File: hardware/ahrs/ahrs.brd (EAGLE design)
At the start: 32 x 30 mm, 38 parts, among them J1 2-PIN, J2 3-PIN3, J3 SM08B-SRSS-TB, U1 LSM9DS1, U2 STM32G4_UFQFPN48_T1, U3 LDFM33PUR, U4 MCP2542FD, X1 NX2016SA24MHZ-EXS00A-CS11335

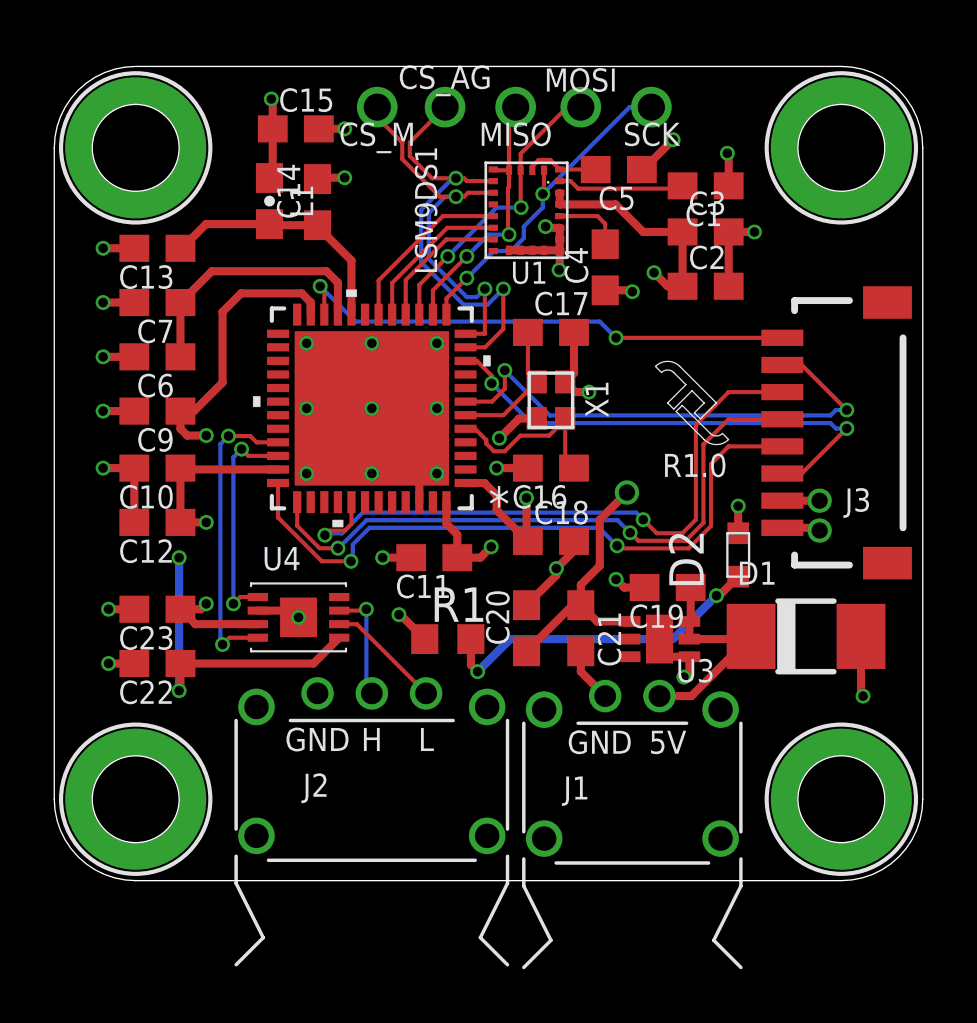
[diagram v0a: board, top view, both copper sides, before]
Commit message: Added LEDs and updates for PCBway
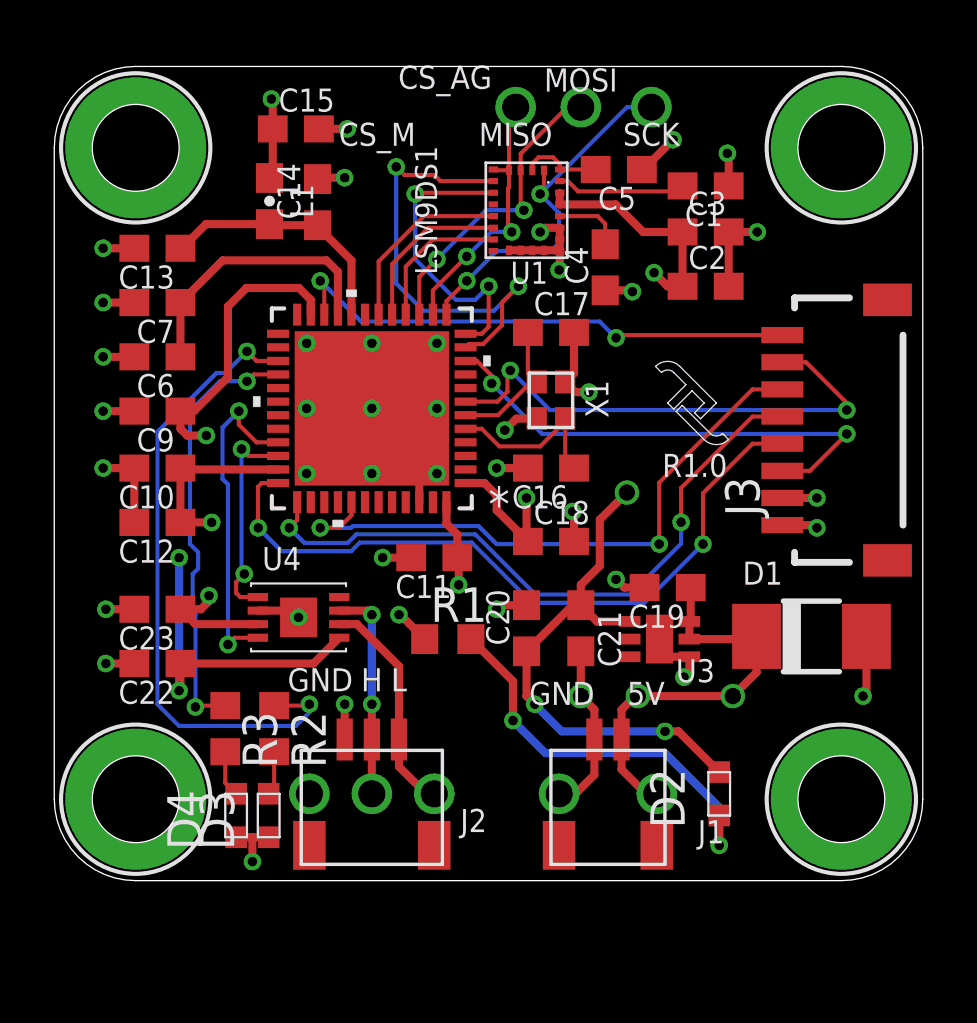
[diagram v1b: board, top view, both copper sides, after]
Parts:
- added D3, D4: LED_0603150060RS75000, timlib:D0603
- added R2, R3: 68, rcl:R0603
- J1: value 2-PIN -> LINEAR_2_JST_SH_RA; device timlib:M80-8420242 -> _T_conn:JST_SM02B-SRSS-TB
- J2: value 3-PIN3 -> LINEAR_3_JST_PH_RA; device timlib:M80-8430342 -> _T_conn:JST_SM03B-SRSS-TB
- J3: value SM08B-SRSS-TB -> LINEAR_8_JST_PH_RA; device timlib:SM08B-SRSS-TB -> _T_conn:JST_SM08B-SRSS-TB
- moved D2 8.83 mm to (24.5, 3.20)
- moved J1 2.56 mm to (20.4, 4.40)
- moved J2 2.50 mm to (11.7, 4.40)
- moved D1 0.20 mm to (27.9, 9.00)
- moved J3 0.10 mm to (29.8, 16.6)
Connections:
- new net N$10: R3.1, U2.28
- new net N$7: R2.1, U2.27
- new net N$8: D3.2, R2.2
- new net N$9: D4.2, R3.2
- net GND: now also D3.1, D4.1
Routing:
- net N$7: track 0.00 -> 23.6 mm, vias 0 -> 2
- net N$10: track 0.00 -> 16.1 mm, vias 0 -> 2
- net 3.3V: track 63.1 -> 72.0 mm, vias 12 -> 13
- net GND: track 47.2 -> 54.4 mm, vias 34 -> 40
- net 5V: track 12.6 -> 19.6 mm, vias 1 -> 4
- net CAN_L: track 4.26 -> 8.26 mm, vias 0 -> 1
- net CAN_H: track 4.20 -> 7.86 mm, vias 1 -> 3
- net CS_M: track 14.4 -> 11.3 mm, vias 3 -> 2
- net N$1: track 12.4 -> 15.1 mm
- net SWDIO: track 24.6 -> 26.6 mm
- net N$9: track 0.00 -> 1.72 mm
- net N$8: track 0.00 -> 1.63 mm
- net SCK: track 12.5 -> 14.0 mm
- net CAN_RX: track 11.2 -> 12.3 mm
- net SWCLK: track 23.4 -> 24.4 mm
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
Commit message: Oops, removed CS_(AG|M) pads
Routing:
- net CS_M: track 11.3 -> 15.5 mm, vias 2 -> 3
- net CS_AG: track 16.7 -> 19.7 mm, vias 2 -> 3
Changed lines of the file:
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@@
 </layers>
 <board>
+<fusionsync huburn="a.YnVzaW5lc3M6Z21haWwyMjE5MTc" projecturn="a.YnVzaW5lc3M6Z21haWwyMjE5MTcjMjAxOTA2MjkyMDE0MTU5NzY" f3durn="urn:adsk.wipprod:dm.lineage:MzfWSGJQS0CBInJEB5SxYw" pcbguid="" lastpulledtime="" lastsyncedchangeguid="" latestrevisionid="cad069d0-54c5-44df-b114-c58309e67b1b" lastsyncedrevisionid="cad069d0-54c5-44df-b114-c58309e67b1b" lastboardhashguid="3784b1de-b935-57e8-db1c-6b4475f25a4e" lastpushedtime="2020-04-26T23:37:28Z" linktopcb3d="%12"/>
 <plain>
 <circle x="3" y="3" radius="2.75" width="0.1524" layer="21"/>
@@
 <circle x="29" y="27" radius="2.75" width="0.1524" layer="21"/>
 <circle x="3" y="27" radius="2.75" width="0.1524" layer="21"/>
-<text x="11.9" y="27.5" size="0.85" layer="25" align="center">CS_M</text>
-<text x="14.4" y="29.6" size="0.85" layer="25" align="center">CS_AG</text>
+<text x="12" y="25.9" size="0.85" layer="25" rot="R90" align="center">CS_M</text>
+<text x="14.4" y="25.7" size="0.85" layer="25" rot="R90" align="center">CS_AG</text>
 <text x="17" y="27.5" size="0.85" layer="25" align="center">MISO</text>
 <text x="19.4" y="29.5" size="0.85" layer="25" align="center">MOSI</text>
@@
 <element name="U1" library="timlib" library_urn="urn:adsk.eagle:library:16152524" package="LGA24_3.5X3X1" package3d_urn="urn:adsk.eagle:package:18130566/2" value="LSM9DS1" x="17.4" y="24.7" smashed="yes" rot="R270">
 <attribute name="NAME" x="17.5" y="22.4" size="0.8128" layer="21" align="center"/>
-<attribute name="VALUE" x="13.7" y="24.7" size="0.8128" layer="21" rot="R270" align="center"/>
 </element>
 <element name="U2" library="timlib" library_urn="urn:adsk.eagle:library:16152524" package="UFQFPN-48_7X7X0P55MM" package3d_urn="urn:adsk.eagle:package:19324073/5" value="STM32G4_UFQFPN48_T1" x="11.7" y="17.4" smashed="yes" rot="R180">
@@
 <via x="17.4" y="14.1" extent="1-16" drill="0.35"/>
 <wire x1="19.4" y1="10.15" x2="19.4" y2="10.9" width="0.3" layer="1"/>
-<wire x1="19.4" y1="10.9" x2="20.1" y2="11.6" width="0.3" layer="1"/>
+<wire x1="19.4" y1="10.9" x2="20.4" y2="11.9" width="0.3" layer="1"/>
 <wire x1="21.2" y1="9.55" x2="20" y2="9.55" width="0.3" layer="1"/>
 <wire x1="20" y1="9.55" x2="19.4" y2="10.15" width="0.3" layer="1"/>
@@
 <wire x1="21.7" y1="26.2" x2="22.8" y2="27.3" width="0.3" layer="1"/>
 <via x="22.8" y="27.3" extent="1-16" drill="0.35"/>
-<wire x1="20.1" y1="13.3" x2="21.1" y2="14.3" width="0.3" layer="1"/>
+<wire x1="20.4" y1="13.6" x2="21.1" y2="14.3" width="0.3" layer="1"/>
 <via x="21.1" y="14.3" extent="1-16" drill="0.6"/>
-<wire x1="20.1" y1="11.6" x2="20.1" y2="13.3" width="0.3" layer="1"/>
+<wire x1="20.4" y1="11.9" x2="20.4" y2="13.6" width="0.3" layer="1"/>
 <contactref element="D2" pad="2"/>
 <wire x1="4.65" y1="8" x2="4.65" y2="7.05" width="0.3" layer="1"/>
@@
 <wire x1="14" y1="26" x2="14.225" y2="25.775" width="0.1524" layer="1"/>
 <wire x1="14.225" y1="25.775" x2="16.175" y2="25.775" width="0.1524" layer="1"/>
+<via x="14.5" y="28.5" extent="1-16" drill="1" alwaysstop="yes"/>
+<wire x1="12.6" y1="26.3" x2="14.5" y2="28.2" width="0.1524" layer="16"/>
+<wire x1="14.5" y1="28.2" x2="14.5" y2="28.5" width="0.1524" layer="16"/>
 </signal>
 <signal name="CS_M">
@@
 <wire x1="16" y1="20.4" x2="15.75" y2="20.15" width="0.1524" layer="1"/>
 <wire x1="15.75" y1="20.15" x2="15.1544" y2="20.15" width="0.1524" layer="1"/>
+<via x="12" y="28.5" extent="1-16" drill="1" alwaysstop="yes"/>
+<wire x1="13.3" y1="25.3" x2="12.4" y2="25.3" width="0.1524" layer="1"/>
+<wire x1="12" y1="25.7" x2="12" y2="28.5" width="0.1524" layer="1"/>
+<wire x1="12.4" y1="25.3" x2="12" y2="25.7" width="0.1524" layer="1"/>
 </signal>
 <signal name="SCK">
@@
 </note>
 <note version="8.3" severity="warning">
+Since Version 8.3, EAGLE supports Fusion synchronisation.
+This feature will not be available in this version and saving
+the document will break the link to the Fusion PCB feature.
+</note>
+<note version="8.3" severity="warning">

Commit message: POSSIBLY BAD MERGE
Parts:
- removed H1, H2, H3, H4: GND_HOLE_M3, timlib:HOLE_GND_M3
- removed J2: LINEAR_3_JST_PH_RA, _T_conn:JST_SM03B-SRSS-TB
- added C8: 0.1uF 10V, _T_rcl:C0603
- added J4: LINEAR_35040500391, _T_conn:MOLEX_5040500391
- added L2: 600R@100MHz, _T_rcl:L0603
- added R4: (no value), _T_rcl:R0603
- C1, C10, C13, C15, C3, C5, C6, C9: value 100nF 10v -> 0.1uF 10V; device rcl:C0603 -> _T_rcl:C0603
- C11, C12, C14, C18, C19, C2, C22, C23, C4, C7: device rcl:C0603 -> _T_rcl:C0603
- C16, C17: value 6.2pF 10v -> 10pF 10v; device rcl:C0603 -> _T_rcl:C0603
- C20, C21: value 22uF 10v -> 2.2uF 10V; device rcl:C0603 -> _T_rcl:C0603
- D1: value SMAJ5A -> (none); device timlib:DO-214AC -> _T_rcl:SOD123
- D2, D3, D4: value LED_0603150060RS75000 -> 150060BS75000; device timlib:D0603 -> _T_rcl:D0603
- J1: value LINEAR_2_JST_SH_RA -> LINEAR_2_5040500291; device _T_conn:JST_SM02B-SRSS-TB -> _T_conn:MOLEX_5040500291
- J3: value LINEAR_8_JST_PH_RA -> LINEAR_85040500891; device _T_conn:JST_SM08B-SRSS-TB -> _T_conn:MOLEX_5040500891
- L1: device timlib:L0603 -> _T_rcl:L0603
- R1, R2, R3: value 68 -> 22; device rcl:R0603 -> _T_rcl:R0603
- U1: device timlib:LGA24_3.5X3X1 -> _T_ic:LGA24_3.5X3X1
- U2: device timlib:UFQFPN-48_7X7X0P55MM -> _T_ic:UFQFPN-48_7X7X0P55MM
- U3: device timlib:DFN6_2X2 -> _T_ic:DFN6_2X2
- U4: device timlib:TDFN_2X3 -> _T_ic:TDFN_2X3
- X1: value NX2016SA24MHZ-EXS00A-CS11335 -> CRYSTAL_NX2016SA-24MHZ-EXS00A-CS11335; device timlib:NX201SA -> _T_ic:NX201SA
- moved D4 22.6 mm to (28.2, 9.50), turned to 0 degrees
- moved D3 22.1 mm to (28.2, 11.2), turned to 0 degrees
- moved R3 18.7 mm to (24.6, 9.50), turned to 0 degrees
- moved R2 17.4 mm to (24.6, 11.2), turned to 0 degrees
- moved C22 16.7 mm to (20.0, 12.2), turned to 270 degrees
- moved J3 16.4 mm to (15.0, 23.6), turned to 0 degrees
- moved U3 15.7 mm to (6.70, 10.3), turned to 270 degrees
- moved C19 15.6 mm to (7.20, 8.20)
- moved C4 11.3 mm to (27.3, 13.7), turned to 0 degrees
- moved R1 10.2 mm to (24.6, 7.80), turned to 180 degrees
- moved C21 9.61 mm to (9.80, 9.80), turned to 180 degrees
- moved C12 9.45 mm to (7.50, 21.9), turned to 270 degrees
- moved U4 9.42 mm to (18.4, 9.10), turned to 90 degrees
- moved C9 8.26 mm to (2.20, 9.20), turned to 0 degrees
- moved C15 8.02 mm to (2.20, 23.3), turned to 180 degrees
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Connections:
- removed net 3.3V: C10.1, C11.1, C12.1, C15.1, C18.1, C2.1, C20.1, C21.1, C22.1, C3.1, C5.1, C9.1, D2.2, J3.1, L1.1, U1.P$22, U1.P$23, U2.1, U2.23, U2.35, U2.48, U3.PIN1, U4.5
- removed net 5V: C19.1, C23.1, D1.C, J1.1, U3.PIN5, U3.PIN6, U4.3
- removed net CAN_H: J2.2, U4.7
- removed net CAN_L: J2.1, U4.6
- removed net INT1_AG: U1.P$11, U2.17
- removed net INT2_AG: U1.P$12, U2.16
- removed net INT_M: U1.P$10, U2.18
- new net +3V3: C10.1, C11.1, C12.1, C15.1, C18.1, C2.1, C20.1, C21.1, C22.1, C3.1, C5.1, C8.1, C9.1, D2.2, J3.P1, L1.1, L2.2, U1.P$22, U1.P$23, U2.1, U2.23, U2.35, U2.48, U3.PIN1, U4.5
- new net +5V: C19.1, C23.1, D1.C, J1.P1, U3.PIN5, U3.PIN6, U4.3
- new net N$11: J4.P1, R4.2, U4.7
- new net N$12: J4.P2, R4.1, U4.6
- net GND: now also C8.2, J1.P2, J3.P2, J4.P3, R2.2, R3.2, U4.8; no longer D3.1, D4.1, H1.P$1, H2.P$1, H3.P$1, H4.P$1, J1.2, J2.3, J3.2
- net LPUART_RX: now also J3.P8; no longer J3.8
- net LPUART_TX: now also J3.P3; no longer J3.3
- net N$10: now also D4.1; no longer U2.28
- net N$7: now also D4.2, U2.28; no longer R2.1, U2.27
- net N$8: now also U2.26; no longer R2.2
- net N$9: now also D3.1, R2.1; no longer D4.2, R3.2
- net NRST: now also J3.P7; no longer J3.7
- net SWCLK: now also J3.P5; no longer J3.5
- net SWDIO: now also J3.P4; no longer J3.4
- net SWO: now also J3.P6; no longer J3.6
- net VDDA: now also L2.1
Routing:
- net 3.3V: track 72.0 -> 0.00 mm, vias 13 -> 0
- net +3V3: track 0.00 -> 50.7 mm, vias 0 -> 14
- net N$8: track 1.63 -> 43.2 mm, vias 0 -> 2
- net +5V: track 0.00 -> 33.9 mm
- net 5V: track 19.6 -> 0.00 mm, vias 4 -> 0
- net N$7: track 23.6 -> 42.3 mm
- net N$10: track 16.1 -> 2.05 mm, vias 2 -> 0
- net CAN_TX: track 7.78 -> 21.7 mm
- net N$1: track 15.1 -> 2.05 mm, vias 2 -> 0
- net SWDIO: track 26.6 -> 14.4 mm
- net CS_AG: track 19.7 -> 7.75 mm, vias 3 -> 2
- net CAN_RX: track 12.3 -> 23.2 mm
- net SWCLK: track 24.4 -> 15.6 mm
- net NRST: track 18.8 -> 10.1 mm
- net CS_M: track 15.5 -> 6.90 mm, vias 3 -> 2
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- added copper zone on layer 2, net +3V3
- removed copper zone on layer 2, net 3.3V
- removed copper zone on layer 2, net 5V
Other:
- board size 32 x 30 mm -> 30 x 30 mm
- board text removed: "5V"
- board text removed: "CS_AG"
- board text removed: "CS_M"
- board text removed: "GND"
- board text removed: "H"
- board text removed: "L"
- board text removed: "MISO"
- board text removed: "MOSI"
- board text removed: "R1.0"
- board text removed: "SCK"

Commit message: Initial Power v3
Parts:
- C2: value 10uF 10v -> 10uF 10V
- moved C2 0.10 mm to (27.3, 15.9)
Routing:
- net +3V3: track 50.7 -> 49.9 mm, vias 14 -> 13
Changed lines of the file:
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@@
 </layers>
 <board>
-<fusionsync huburn="a.YnVzaW5lc3M6Z21haWwyMjE5MTc" projecturn="a.YnVzaW5lc3M6Z21haWwyMjE5MTcjMjAxOTA2MjkyMDE0MTU5NzY" f3durn="urn:adsk.wipprod:dm.lineage:MzfWSGJQS0CBInJEB5SxYw" pcbguid="" lastpulledtime="" lastsyncedchangeguid="" latestrevisionid="2e79b3d6-53ce-43aa-848e-6e5a329550ac" lastsyncedrevisionid="2e79b3d6-53ce-43aa-848e-6e5a329550ac" lastboardhashguid="9ffdacb0-3b78-cc97-8a35-4617afdf7dd1" lastpushedtime="2020-06-01T07:50:32Z" linktopcb3d="%12"/>
+<fusionsync huburn="a.YnVzaW5lc3M6Z21haWwyMjE5MTc" projecturn="a.YnVzaW5lc3M6Z21haWwyMjE5MTcjMjAxOTA2MjkyMDE0MTU5NzY" f3durn="urn:adsk.wipprod:dm.lineage:MzfWSGJQS0CBInJEB5SxYw" pcbguid="" lastpulledtime="" lastsyncedchangeguid="" latestrevisionid="479aee42-1d56-4d93-9275-ec8a74ec2958" lastsyncedrevisionid="479aee42-1d56-4d93-9275-ec8a74ec2958" lastboardhashguid="e3f8bce3-a763-ae1a-6ea7-c9e59d677afc" lastpushedtime="2020-06-02T04:09:23Z" linktopcb3d="%12"/>
 <plain>
 <circle x="3" y="3" radius="2.75" width="0.1524" layer="21"/>
@@
 <attribute name="VALUE" x="2.835" y="25.205" size="1.27" layer="27" rot="R180"/>
 </element>
-<element name="C2" library="_T_rcl" library_urn="urn:adsk.eagle:library:19571919" package="C0603" package3d_urn="urn:adsk.eagle:package:19572011/3" override_package3d_urn="urn:adsk.eagle:package:19477979/2" override_package_urn="urn:adsk.eagle:footprint:23123/1" override_locally_modified="yes" value="10uF 10v" x="27.3" y="15.8" smashed="yes" rot="R180">
-<attribute name="NAME" x="29.1" y="15.8" size="0.8" layer="25" rot="R180" align="center"/>
-<attribute name="VALUE" x="27.935" y="17.705" size="1.27" layer="27" rot="R180"/>
-</element>
 <element name="C3" library="_T_rcl" library_urn="urn:adsk.eagle:library:19571919" package="C0603" package3d_urn="urn:adsk.eagle:package:19572011/3" value="0.1uF 10V" x="27.3" y="17.8" smashed="yes" rot="R180">
 <attribute name="NAME" x="29.1" y="17.8" size="0.8" layer="25" rot="R180" align="center"/>
@@
 <attribute name="NAME" x="19.97" y="2.07" size="0.8" layer="25" rot="R180" align="center"/>
 <attribute name="VALUE" x="19.97" y="3.67" size="0.9" layer="27" rot="R180" align="center"/>
+</element>
+<element name="C2" library="_T_rcl" library_urn="urn:adsk.eagle:library:19571919" package="C0603" package3d_urn="urn:adsk.eagle:package:19572011/3" value="10uF 10V" x="27.3" y="15.9" smashed="yes" rot="R180">
+<attribute name="NAME" x="29.17" y="15.93" size="0.8" layer="25" rot="R180" align="center"/>
+<attribute name="VALUE" x="28.57" y="18.44" size="1.27" layer="27" rot="R180"/>
 </element>
 </elements>
@@
 <contactref element="U1" pad="P$16"/>
 <contactref element="U1" pad="P$18"/>
-<contactref element="C2" pad="2"/>
 <contactref element="C3" pad="2"/>
 <contactref element="X1" pad="P$4"/>
@@
 <via x="3.7" y="23.3" extent="1-16" drill="0.29"/>
 <wire x1="1.45" y1="17.4" x2="1.45" y2="19.5" width="0.3" layer="1"/>
-<wire x1="1.45" y1="17.4" x2="0.5474" y2="17.4" width="0.3" layer="1"/>
-<via x="0.5474" y="17.4" extent="1-16" drill="0.29"/>
-<wire x1="28.05" y1="15.8" x2="28.05" y2="17.8" width="0.3" layer="1"/>
+<wire x1="1.45" y1="17.4" x2="0.7" y2="17.4" width="0.3" layer="1"/>
+<via x="0.7" y="17.4" extent="1-16" drill="0.29"/>
 <wire x1="28.05" y1="17.8" x2="28.05" y2="18.65" width="0.3" layer="1"/>
 <wire x1="28.05" y1="18.65" x2="28.2" y2="18.8" width="0.3" layer="1"/>
@@
 <wire x1="18.225" y1="18.475" x2="18.225" y2="19.375" width="0.3" layer="1"/>
 <wire x1="18.225" y1="19.375" x2="18.55" y2="19.7" width="0.3" layer="1"/>
+<contactref element="C2" pad="2"/>
+<wire x1="28.05" y1="15.9" x2="28.05" y2="17.8" width="0.3" layer="1"/>
 </signal>
 <signal name="N$2">
@@
 <contactref element="L1" pad="1"/>
 <contactref element="U1" pad="P$22"/>
-<contactref element="C2" pad="1"/>
 <contactref element="C3" pad="1"/>
 <contactref element="U1" pad="P$23"/>
@@
 <wire x1="28.1" y1="22.05" x2="28.1" y2="21.1" width="0.3" layer="1"/>
 <via x="28.1" y="21.1" extent="1-16" drill="0.29"/>
-<wire x1="26.55" y1="17.8" x2="26.55" y2="15.8" width="0.3" layer="1"/>
-<wire x1="26.55" y1="15.8" x2="25.8" y2="15.8" width="0.3" layer="1"/>
-<via x="25.8" y="15.8" extent="1-16" drill="0.29"/>
 <wire x1="1.45" y1="11.3" x2="1.45" y2="13.3" width="0.3" layer="1"/>
 <wire x1="5.3" y1="21.15" x2="5.05" y2="21.15" width="0.3" layer="1"/>
@@
 <wire x1="2.95" y1="8.55" x2="3.3" y2="8.2" width="0.3" layer="1"/>
 <via x="3.3" y="8.2" extent="1-16" drill="0.29"/>
+<contactref element="C2" pad="1"/>
+<wire x1="26.55" y1="15.9" x2="26.55" y2="17.8" width="0.3" layer="1"/>
+<wire x1="28.1" y1="21.1" x2="26.55" y2="17.8" width="0" layer="19" extent="1-1"/>
 </signal>
 <signal name="N$7">
@@
 packages will not be understood (or retained) with this version.
 </note>
-<note version="9.4" severity="warning">
-Since Version 9.4, EAGLE supports the overriding of 3D packages
-in schematics and board files. Those overridden 3d packages
-will not be understood (or retained) with this version.
-</note>
 </compatibility>
